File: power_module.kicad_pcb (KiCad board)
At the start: 4 copper layers, 95 x 76.9 mm, 71 parts, among them J1 USB_C_PD, J2 OUTPUT, J3 I2C_BREAKOUT, Q1 DUAL_N_FET, Q2 DUAL_N_FET, Q3 DUAL_N_FET, Q4 DUAL_N_FET, SW1 ON_OFF, U1 BQ7692003, U2 CH224K, U3 BQ24650, U4 LM5176PWPR

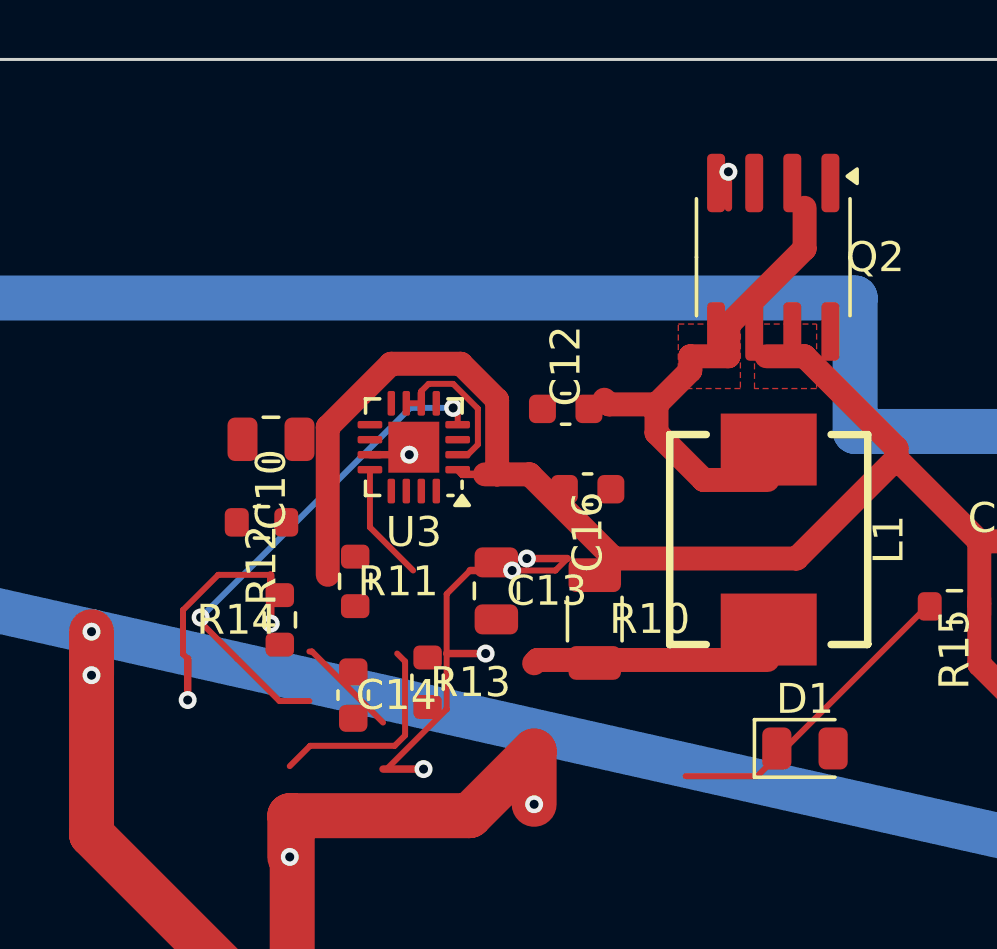
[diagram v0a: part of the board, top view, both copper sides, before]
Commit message: charger: incremental autoroute of 6/8 BQ signal nets
First use of the new incremental autoroute (MCP #242): routed
BQ_PH/BQ_VREF/BQ_VFB/BQ_BTST/BQ_LODRV/CHG_OUT (+69 tracks, +5 vias),
leaving all non-charger copper byte-identical. refill_zones run after.

Hand-off state for review: BQ_HIDRV and BQ_STAT1 still open, and ~8
clashes remain where the freshly-routed charger tracks meet the existing
USB_VBUS pour / fixed pads (the incremental-route caveat — freerouting
optimized against a re-routed scratch layout). DRC 108 total.

(.kicad_sch: verify_netclass_patterns bootstrapped the
mcp_expected_netclass_patterns metadata property — purely additive.)
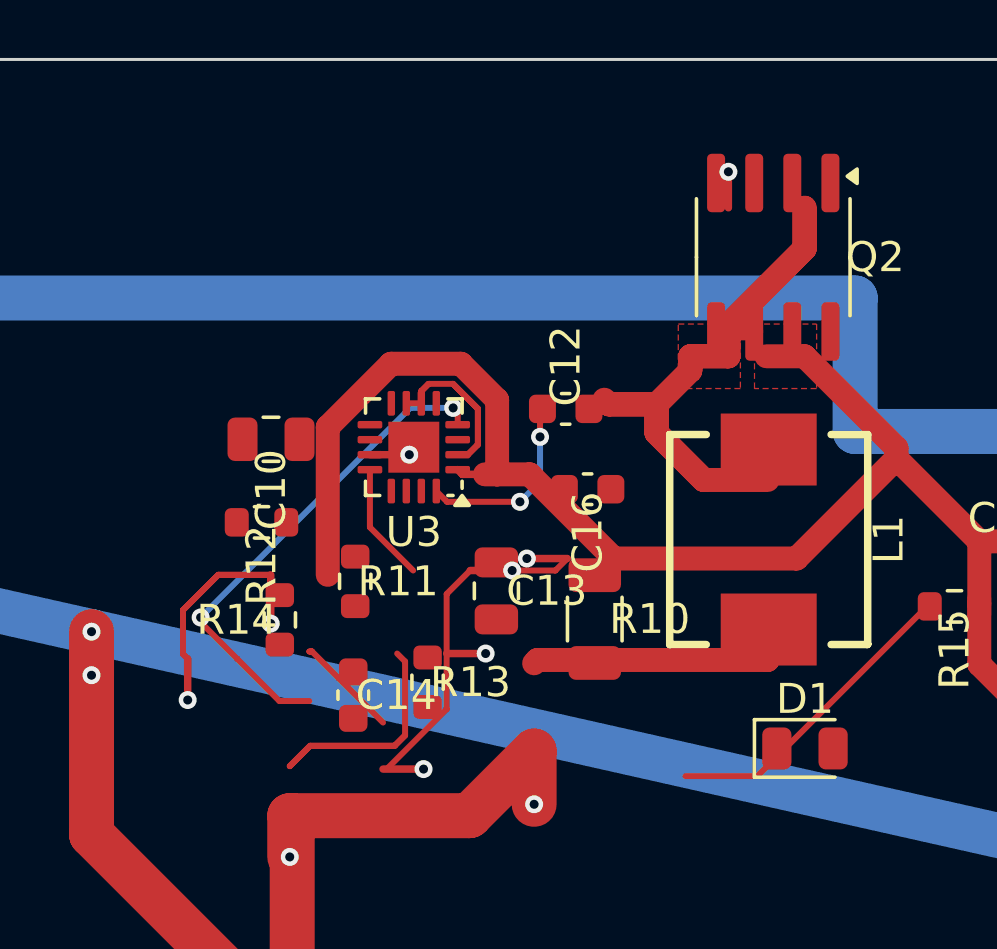
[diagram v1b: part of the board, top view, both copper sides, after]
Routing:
- net BQ_PH: track 16.4 -> 29.9 mm
- net BQ_VFB: track 15.2 -> 23.1 mm
- net BQ_BTST: track 0.00 -> 6.34 mm, vias 0 -> 2
- net BQ_VREF: track 8.68 -> 13.3 mm
- net CHG_OUT: track 7.83 -> 8.86 mm

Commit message: Claude did some re-placing
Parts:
- moved C15 39.4 mm to (47.5, 22.1)
- moved C10 11.7 mm to (51.2, 7.89)
- moved Q2 7.77 mm to (64.6, 9.31)
- moved C12 5.20 mm to (55.4, 10.4)
- moved R11 4.77 mm to (40.8, 13.4), turned to 180 degrees
- moved R12 4.74 mm to (40.7, 10.8)
- moved C14 3.97 mm to (42.3, 17.4)
- moved R13 3.83 mm to (41.9, 21.2)
- moved C16 3.76 mm to (51.5, 10.6)
- moved R10 3.23 mm to (49.2, 16.2)
- moved C13 3.03 mm to (45.0, 17.8)
- moved R14 3.02 mm to (39.2, 16.2), turned to 0 degrees
- moved D1 1.59 mm to (58.5, 21.4)
- moved L1 1.12 mm to (56.1, 15.7), turned to 180 degrees
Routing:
- net BQ_PH: track 29.9 -> 7.27 mm
- net USB_VBUS: track 104.6 -> 83.8 mm
- net BQ_VFB: track 23.1 -> 4.94 mm, vias 2 -> 0
- net GND: track 107.0 -> 88.9 mm, vias 33 -> 29
- net BAT+: track 108.7 -> 122.3 mm, vias 17 -> 21
- net BQ_VREF: track 13.3 -> 0.50 mm
- net BQ_TS: track 16.8 -> 10.1 mm
- net BQ_BTST: track 6.34 -> 0.00 mm, vias 2 -> 0
- net CHG_OUT: track 8.86 -> 4.05 mm, vias 0 -> 2
- net LED_A: track 10.5 -> 8.13 mm
- net BQ_LODRV: track 1.61 -> 0.00 mm, vias 1 -> 0
